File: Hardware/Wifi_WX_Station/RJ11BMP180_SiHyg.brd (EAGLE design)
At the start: 24.8 x 20 mm, 8 parts, among them U1 SI7021-DFN6

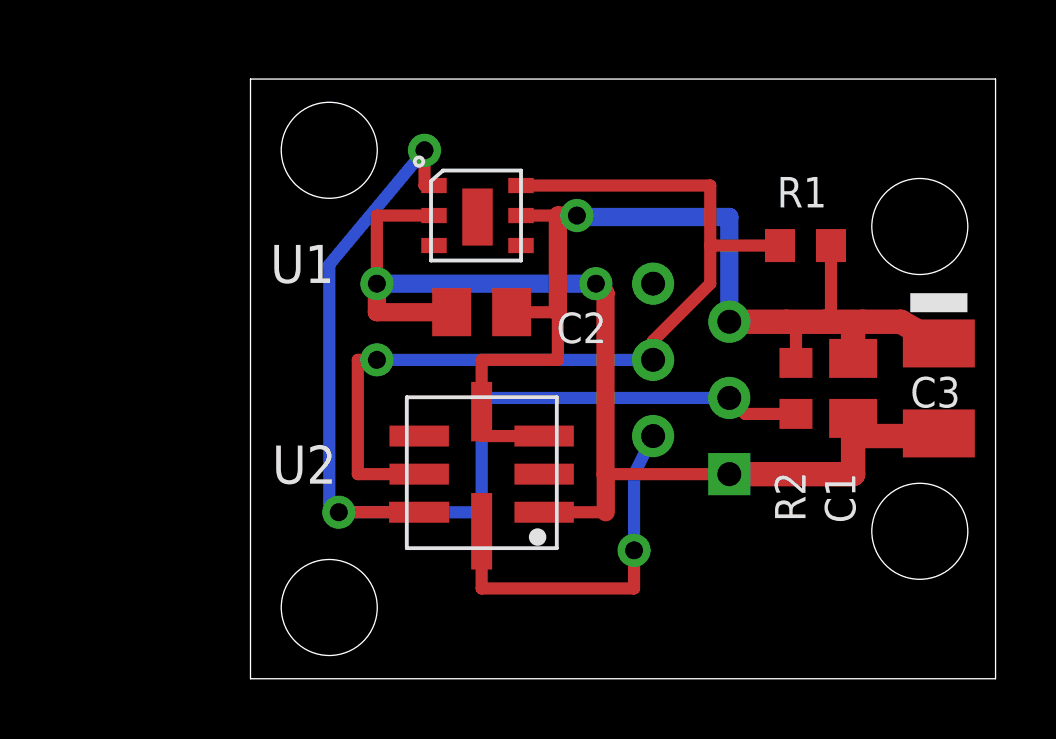
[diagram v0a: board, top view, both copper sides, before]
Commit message: added PCB for BOSH PMP180 revised WE28 schemaitc with added text
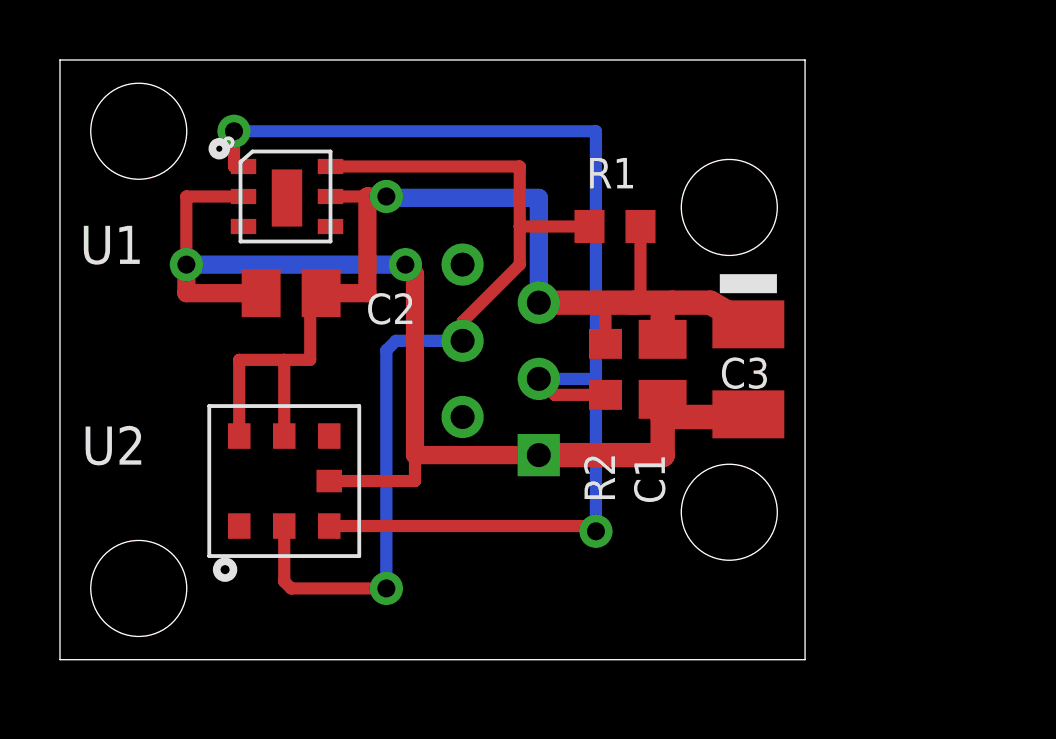
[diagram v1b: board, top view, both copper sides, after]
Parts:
- removed U2: (no value), 1AA_Stofer:LCC8
- added U$2: BMP180LDA_7, 1AA_Stofer:LGA_7
- moved C3 6.38 mm to (22.9, 9.84)
- moved R1 6.38 mm to (18.4, 14.6)
- moved R2 6.38 mm to (18.1, 9.84)
- moved C2 6.38 mm to (7.62, 12.4)
- moved U1 6.38 mm to (6.03, 14.6)
- moved C1 6.38 mm to (20.0, 9.84)
- moved JP2 6.38 mm to (23.5, 10.2)
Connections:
- removed net XCLR: JP2.P$2, U2.P$8
- net +3V3: now also U$2.P$2, U$2.P$3; no longer U2.P$3, U2.P$4
- net GND: now also U$2.P$7; no longer U2.P$1
- net SCL: now also U$2.P$5; no longer U2.P$6
- net SDA: now also U$2.P$6; no longer U2.P$7
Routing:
- net XCLR: track 12.2 -> 0.00 mm, vias 1 -> 0
- net SDA: track 36.8 -> 40.2 mm
- net +3V3: track 37.3 -> 38.4 mm
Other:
- board text added: "Rev B.3"
- board text added: "Wunder Weather 2015"
- board text removed: "Rev B.2"
- board text removed: "Wunder Weather 2014"
